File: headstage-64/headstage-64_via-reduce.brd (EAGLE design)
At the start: 19.3 x 19 mm, 172 parts, among them U1 TS4231, U11 10M08DC, U12 LT3463, U13 DAC5311, U14 TS4231, U15 INA826, U16 TLV70733, U17 TLV70712, U18 TLV70733, U19 DS90UB913A_WQFN, U2 MPU9250_QFN_NO-PAD, U22 TPS62621, U25 TPL0501_UQFN, U26 ASCO-50.000MHZ-EK-T3, U3 CAT4016_QFN, U4 OPA170, U5 TS4231, U6 TS4231, U7 RHD2064_BGA, U8 ADG1401, U9 TLV70725

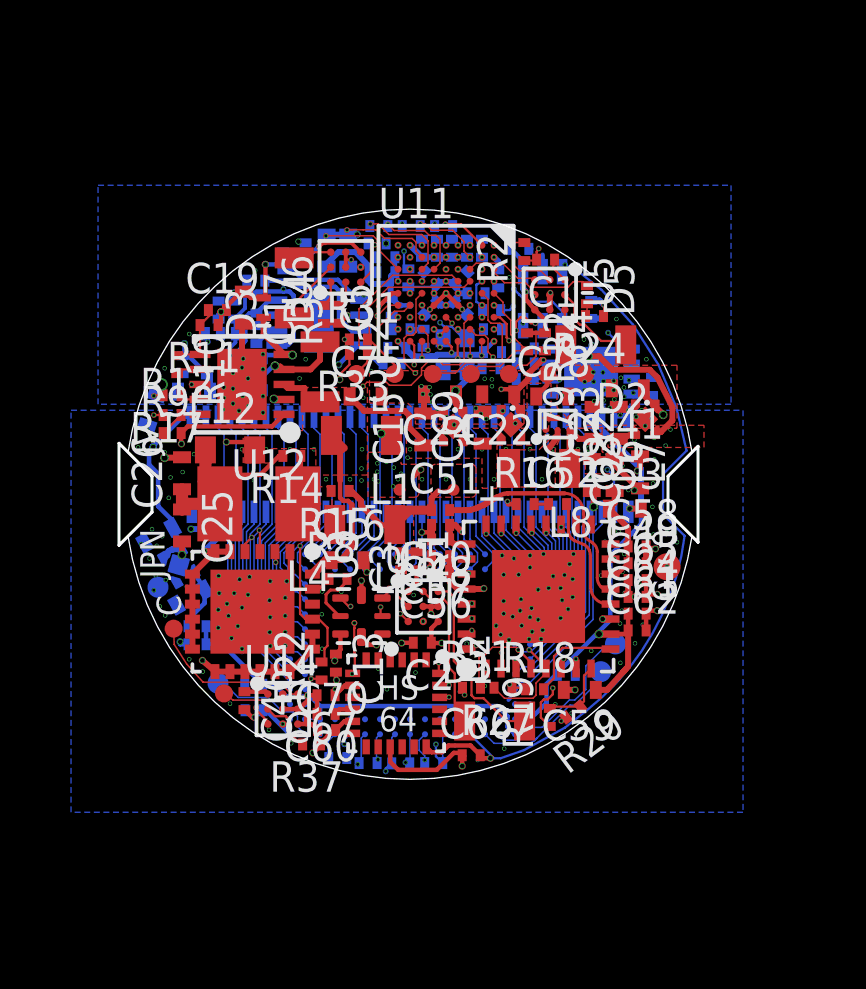
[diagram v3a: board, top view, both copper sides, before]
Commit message: Finalizing headstage-64
- Jon's final edits before fab
- Daughter board switched to IPEC4 coax connector
- RF grounding improvements: controlled impedance on daughter board and
mainboard.
- Lots of small routing improvments for DRC etc
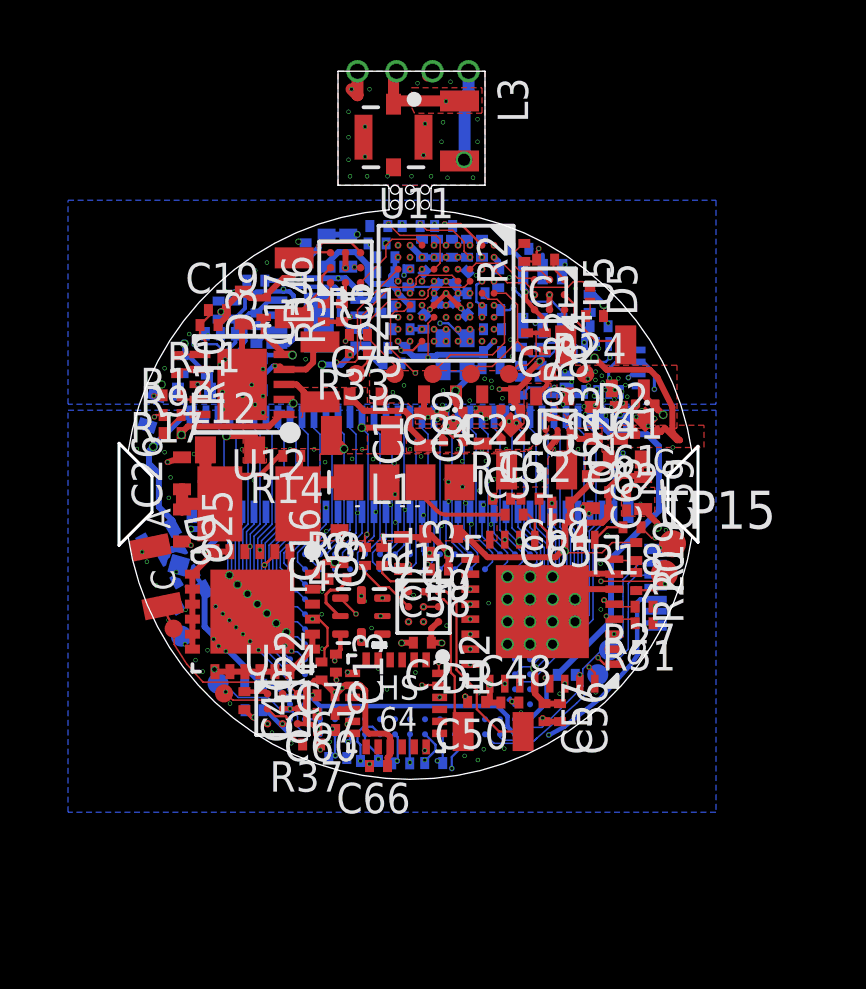
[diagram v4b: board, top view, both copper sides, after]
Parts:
- removed CENTER, SHIELD: (no value), jonnew:B0.4MM
- removed R39: 0 (DNP), jonnew:0201T
- removed R40: 0, jonnew:0201T
- added D6: VEMD1160X01, jonnew:0805T
- added J1: (no value), jonnew:X_FL_R_SMT_1(02)
- added J2: (no value), jonnew:HEADSTAGE64-DAUGHER-CARD-CASTELLATED
- added J3: (no value), jonnew:HEADSTAGE-64-DAUGHTER-CARD
- added R25: 10k, jonnew:0201T
- added TP15: (no value), jonnew:TP09R
- added U$54: PINHD-1X5_HALF_CONNETOR, jonnew:DF40-10HEAD_HALF
- R13: value 49.9 -> 590
- U8: value ADG1401 -> DG509B; device jonnew:LFCSP8-2X3 -> jonnew:MQFN16-1.8X2.6
- moved R15 13.6 mm to (1.52, 13.1), flipped to the bottom
- moved L3 13.5 mm to (1.65, 12.1), turned to 270 degrees
- moved C53 7.54 mm to (-0.23, -1.96), turned to 270 degrees
- moved C59 6.89 mm to (7.77, 0.04), turned to 270 degrees
- moved C58 6.63 mm to (0.98, -2.51), turned to 180 degrees
- moved C49 6.60 mm to (0.98, -1.95), turned to 180 degrees
- moved R18 6.30 mm to (7.40, -1.10), turned to 180 degrees
- moved C57 6.26 mm to (4.48, -7.28), turned to 270 degrees
- moved R19 6.24 mm to (7.54, -1.91), turned to 270 degrees
- moved C56 6.18 mm to (5.00, -7.28), turned to 270 degrees
- moved R51 6.14 mm to (7.80, -4.30), turned to 180 degrees
- moved L7 6.10 mm to (1.04, -1.32), turned to 180 degrees
- moved C50 6.02 mm to (2.22, -6.92)
- moved C48 5.91 mm to (3.33, -6.94), turned to 0 degrees
- moved R27 5.42 mm to (7.80, -3.75)
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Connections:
- net RHD_CLK_+ renamed RHD_CLK_P
- net RHD_CLK_- renamed RHD_CLK_N
- net RHD_CS_+ renamed RHD_CS_P
- net RHD_CS_- renamed RHD_CS_N
- net RHD_MISO_+ renamed RHD_MISO_P
- net RHD_MISO_- renamed RHD_MISO_N
- net RHD_MOSI_+ renamed RHD_MOSI_P
- net RHD_MOSI_- renamed RHD_MOSI_N
- removed net INTAN_VDD: C73.2, R39.1, R40.2, U7.M15, U7.M16, U7.N15, U7.N2
- removed net V+: C10.1, C18.1, C20.1, C7.1, R9.2, U12.1, U15.8, U4.5, U8.4
- removed net V-: C11.1, C17.1, C19.2, C21.1, C8.1, D4.A, R11.1, U15.5, U15.PAD, U4.2, U8.7, U8.PAD
- new net +15V: C10.1, C18.1, C20.1, C7.1, R9.2, U12.1, U15.8, U4.5, U8.12
- new net -15V: C11.1, C17.1, C19.2, C21.1, C8.1, D4.A, R11.1, U15.5, U15.PAD, U4.2, U8.1
- new net GND1: J1.P$2, J1.P$3, J1.P$4, J2.2, J2.4
- new net ISTIM_MONO: C9.1, R4.1, R5.2, U4.3, U7.N5
- new net ISTIM_PRE: R7.1, U15.1, U8.7
- new net N$44: R25.2, U8.16
- new net _SIGOUT: J1.P$1, J2.3, L3.1, R15.1
- net +3V3: now also R25.1; no longer R39.2
- net +3V3_AN: now also C73.2, U$54.4, U7.M15, U7.M16, U7.N15, U7.N2; no longer R40.1
- net AGND: now also U$54.M1, U$54.M2
- net AUXIN2: now also U$54.2
- net AUXIN3: now also U$54.1
- net DIN10: now also U11.C5; no longer U11.F8
- net DIN11: now also U11.C4; no longer U11.F9
- net DIN4: now also U11.G8; no longer U11.J7
- net DIN5: now also U11.G9; no longer U11.J8
- net DIN6: now also U11.F7; no longer U11.G7
- net DIN7: now also U11.E7; no longer U11.F7
- net DIN8: now also U11.E8; no longer U11.G8
- net DIN9: now also U11.C8; no longer U11.G9
- net ENV1: now also U11.B5; no longer U11.E8
- net ENV4: now also U11.B7; no longer U11.G3
- net GND: now also J3.2, J3.4, TP15.TP, U8.13, U8.14, U8.2; no longer SHIELD.TP, U8.3
- net GPIO0: now also U$54.3
- net HSYNC: now also U11.F2; no longer U11.B7
- net IMU_CS: now also U11.F9; no longer U11.A3
- net ISTIM: now also U8.10, U8.6; no longer R7.1, U15.1, U8.1
- net LED_BLANK: now also U11.C9; no longer U11.C5
- net LED_CLK: now also U11.J7; no longer U11.F2
- net LED_LATCH: now also U11.J8; no longer U11.G2
- net MIDFILT: now also J3.1; no longer L3.2, R15.2
- net N$23: now also U8.11; no longer U8.8
- net N$25: now also J2.1, L3.2, R15.2; no longer C9.1, R4.1, R5.2, U4.3
- net N$26: now also D6.2
- net N$38: now also D6.1
- net PCLK: now also U11.G2; no longer U11.C9
- net POT_CS: now also U11.G7; no longer U11.G1
- net SCL: now also U11.G3; no longer U11.C8
- net SDA: now also U11.F8; no longer U11.E7
- net SDI: now also U11.C7; no longer U11.B5
- net SIGOUT: now also J3.3; no longer CENTER.TP, L3.1, R15.1
- net STIM_NULL: now also U11.A3, U8.15; no longer U11.C4, U8.6
- net VDAC: no longer U7.N5
- net VSYNC: now also U11.G1; no longer U11.C7
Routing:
- net +15V: track 0.00 -> 35.2 mm, vias 0 -> 4
- net V+: track 34.1 -> 0.00 mm, vias 4 -> 0
- net ISTIM_MONO: track 0.00 -> 29.4 mm, vias 0 -> 3
- net GPIO0: track 18.8 -> 44.0 mm, vias 3 -> 4
- net VDAC: track 38.2 -> 15.4 mm
- net V-: track 22.3 -> 0.00 mm, vias 4 -> 0
- net +3V3_AN: track 2.15 -> 23.2 mm, vias 0 -> 2
- net -15V: track 0.00 -> 20.7 mm, vias 0 -> 4
- net ENV1: track 13.8 -> 34.4 mm
- net DIN9: track 11.7 -> 31.6 mm
- net ISTIM_PRE: track 0.00 -> 19.4 mm, vias 0 -> 2
- net DIN8: track 11.1 -> 30.4 mm
- net DIN7: track 10.4 -> 28.2 mm
- net ISTIM: track 25.5 -> 8.72 mm, vias 3 -> 2
- net DATA1: track 14.3 -> 30.8 mm, vias 3 -> 2
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- added copper zone on layer 7, net $N324
- added copper zone on layer 1, net +15V
- added copper zone on layer 16, net +15V
- added copper zone on layer 3, net +15V
- added copper zone on layer 7, net +1V2
- added copper zone on layer 7, net +2V5
- added copper zone on layer 7, net +3V3
- added copper zone on layer 16, net +3V3_AN
- added copper zone on layer 7, net +3V3_AN
- added copper zone on layer 1, net -15V
- added copper zone on layer 16, net -15V
- added copper zone on layer 3, net -15V
- added copper zone on layer 7, net AGND
- added copper zone on layer 5, net DAC_CS
- added copper zone on layer 5, net DATA4
- added copper zone on layer 5, net DIN0
- added copper zone on layer 5, net DIN1
- added copper zone on layer 5, net DIN10
- added copper zone on layer 5, net DIN11
- added copper zone on layer 5, net DIN2
- added copper zone on layer 5, net DIN3
- added copper zone on layer 5, net DIN4
- added copper zone on layer 5, net DIN5
- added copper zone on layer 5, net DIN6
- added copper zone on layer 5, net DIN7
- added copper zone on layer 5, net DIN8
- added copper zone on layer 5, net DIN9
- added copper zone on layer 3, net ENV1
- added copper zone on layer 5, net ENV2
- added copper zone on layer 5, net ENV3
- added copper zone on layer 5, net ENV4
- added copper zone on layer 2, net GND
- added copper zone on layer 6, net GND
- added copper zone on layer 1, net GND1
- added copper zone on layer 16, net GND1
- added copper zone on layer 4, net GND1
- added copper zone on layer 7, net GND1
- added copper zone on layer 16, net GPIO0
- added copper zone on layer 5, net GPIO0
- added copper zone on layer 5, net HSYNC
- added copper zone on layer 5, net IMU_CS
- added copper zone on layer 5, net ISTIM
- added copper zone on layer 16, net ISTIM_MONO
- added copper zone on layer 3, net ISTIM_MONO
- added copper zone on layer 5, net ISTIM_MONO
- added copper zone on layer 16, net ISTIM_PRE
- added copper zone on layer 3, net ISTIM_PRE
- added copper zone on layer 5, net LED_BLANK
- added copper zone on layer 5, net LED_CLK
- added copper zone on layer 5, net LED_LATCH
- added copper zone on layer 16, net N$23
- added copper zone on layer 7, net N$23
- added copper zone on layer 1, net N$25
- added copper zone on layer 16, net N$25
- added copper zone on layer 1, net N$35
- added copper zone on layer 3, net N$35
- added copper zone on layer 5, net N$37
- added copper zone on layer 1, net N$38
- added copper zone on layer 5, net N$38
- added copper zone on layer 1, net N$43
- added copper zone on layer 4, net N$43
- added copper zone on layer 5, net N$45
- added copper zone on layer 2, net N$47
- added copper zone on layer 3, net N$47
- added copper zone on layer 4, net N$47
- added copper zone on layer 5, net PCLK
- added copper zone on layer 5, net POT_CS
- added copper zone on layer 3, net RHD_CLK_N
- added copper zone on layer 5, net RHD_CLK_N
- added copper zone on layer 3, net RHD_CLK_P
- added copper zone on layer 5, net RHD_CLK_P
- added copper zone on layer 3, net RHD_CS_N
- added copper zone on layer 3, net RHD_CS_P
- added copper zone on layer 3, net RHD_MISO_N
- added copper zone on layer 3, net RHD_MISO_P
- added copper zone on layer 3, net RHD_MOSI_N
- added copper zone on layer 3, net RHD_MOSI_P
- added copper zone on layer 5, net SCL
- added copper zone on layer 3, net SDA
- added copper zone on layer 5, net SDI
- added copper zone on layer 5, net STIM_NULL
- added copper zone on layer 5, net VCOAX
- added copper zone on layer 7, net VDAC
- added copper zone on layer 5, net VSYNC
- added copper zone on layer 1, net _SIGOUT
- added copper zone on layer 16, net _SIGOUT
- removed copper zone on layer 5, net $N324
- removed copper zone on layer 5, net +1V2
- removed copper zone on layer 5, net +3V3
- removed copper zone on layer 5, net AGND
- removed copper zone on layer 2, net DAC_CS
- removed copper zone on layer 1, net DATA1
- removed copper zone on layer 2, net DATA1
- removed copper zone on layer 1, net DATA3
- removed copper zone on layer 2, net DATA3
- removed copper zone on layer 2, net DATA4
- removed copper zone on layer 1, net DIN0
- removed copper zone on layer 2, net DIN0
- removed copper zone on layer 1, net DIN1
- removed copper zone on layer 2, net DIN1
- removed copper zone on layer 2, net DIN10
- removed copper zone on layer 2, net DIN11
- removed copper zone on layer 2, net DIN2
- removed copper zone on layer 1, net DIN3
- removed copper zone on layer 2, net DIN3
- removed copper zone on layer 1, net DIN4
- removed copper zone on layer 2, net DIN4
- removed copper zone on layer 1, net DIN5
- removed copper zone on layer 2, net DIN5
- removed copper zone on layer 2, net DIN6
- removed copper zone on layer 1, net DIN7
- removed copper zone on layer 2, net DIN7
- removed copper zone on layer 2, net DIN8
- removed copper zone on layer 1, net DIN9
- removed copper zone on layer 2, net DIN9
- removed copper zone on layer 2, net ENV1
- removed copper zone on layer 1, net ENV2
- removed copper zone on layer 2, net ENV2
- removed copper zone on layer 2, net ENV3
- removed copper zone on layer 1, net ENV4
- removed copper zone on layer 2, net ENV4
- removed copper zone on layer 3, net ENV4
- removed copper zone on layer 2, net GPIO0
- removed copper zone on layer 3, net GPIO0
- removed copper zone on layer 2, net HSYNC
- removed copper zone on layer 1, net IMU_CS
- removed copper zone on layer 3, net IMU_CS
- removed copper zone on layer 3, net ISTIM
- removed copper zone on layer 3, net LED_BLANK
- removed copper zone on layer 3, net LED_CLK
- removed copper zone on layer 3, net LED_LATCH
- removed copper zone on layer 1, net MIDFILT
- removed copper zone on layer 2, net MOSI
- removed copper zone on layer 1, net N$34
- removed copper zone on layer 3, net N$34
- removed copper zone on layer 2, net N$37
- removed copper zone on layer 3, net N$43
- removed copper zone on layer 2, net N$45
- removed copper zone on layer 2, net PCLK
- removed copper zone on layer 1, net POT_CS
- removed copper zone on layer 2, net POT_CS
- removed copper zone on layer 3, net POT_CS
- removed copper zone on layer 1, net RHD_CLK_N
- removed copper zone on layer 2, net RHD_CLK_N
- removed copper zone on layer 2, net RHD_CLK_P
- removed copper zone on layer 1, net RHD_CS_N
- removed copper zone on layer 2, net RHD_CS_N
- removed copper zone on layer 1, net RHD_CS_P
- removed copper zone on layer 2, net RHD_CS_P
- removed copper zone on layer 1, net RHD_MISO_N
- removed copper zone on layer 2, net RHD_MISO_N
- removed copper zone on layer 1, net RHD_MISO_P
- removed copper zone on layer 2, net RHD_MISO_P
- removed copper zone on layer 1, net RHD_MOSI_N
- removed copper zone on layer 2, net RHD_MOSI_N
- removed copper zone on layer 1, net RHD_MOSI_P
- removed copper zone on layer 2, net RHD_MOSI_P
- removed copper zone on layer 2, net SCL
- removed copper zone on layer 2, net SCLK
- removed copper zone on layer 2, net SDA
- removed copper zone on layer 2, net SDI
- removed copper zone on layer 1, net SIGOUT
- removed copper zone on layer 2, net STIM_NULL
- removed copper zone on layer 1, net V+
- removed copper zone on layer 16, net V+
- removed copper zone on layer 3, net V+
- removed copper zone on layer 1, net V-
- removed copper zone on layer 16, net V-
- removed copper zone on layer 3, net V-
- removed copper zone on layer 5, net VDAC
- removed copper zone on layer 2, net VSYNC
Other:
- board size 19.3 x 19 mm -> 19.3 x 23.6 mm
- board text added: "3"
- board text added: "A"
- board text added: "HS 64 JPN&JV"
- board text removed: "+"
- board text removed: "-"
- board text removed: "IN3"
- board text removed: "JPN"
- board text removed: "JV"

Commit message: headstage-64 ready for fabrication
- Ready for speedy
- Tiny improvements due to DRC and drill rack check
- Fabrication files updated
- Missing gerber files added
- Gerbv project updated
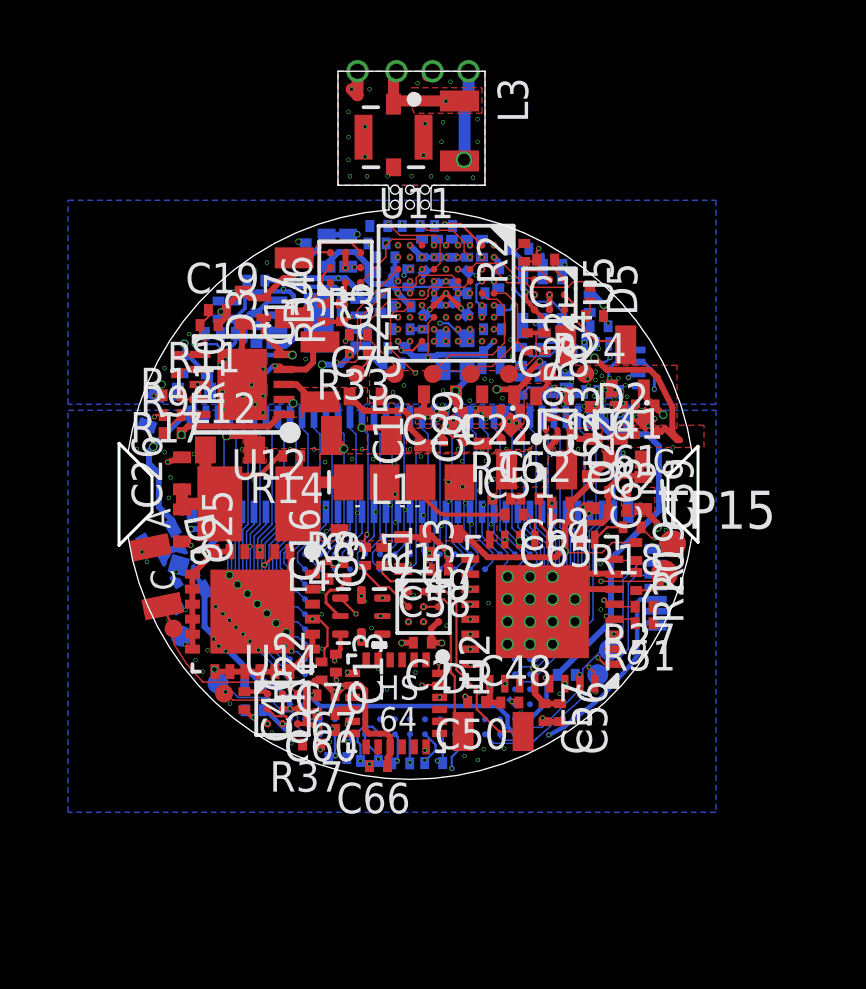
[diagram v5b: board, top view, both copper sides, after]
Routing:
- net GND: vias 201 -> 200
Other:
- board text added: "HS-64 Rev 1.2"
- board text removed: "HS-64 Rev 1.1"

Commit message: Moved parts around on headstage-64 to increase spaces between pads
- Tried to jiggle parts around to prevent very closely spaced pads on
difference signals. Hopefully this will reduce possibily of shorts
during reflow.
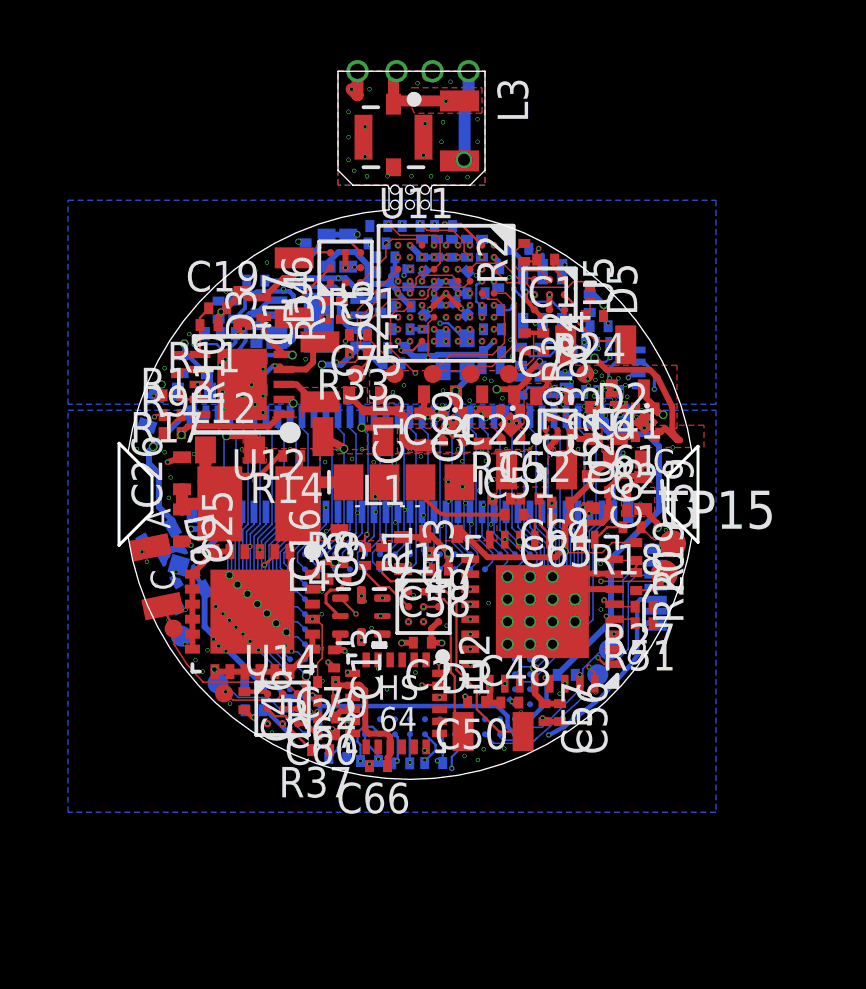
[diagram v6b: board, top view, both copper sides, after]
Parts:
- moved R22 0.41 mm to (-2.78, -6.26), turned to 180 degrees
- moved R37 0.36 mm to (-2.98, -8.53)
- moved L1 0.28 mm to (-1.90, 1.92)
- moved C67 0.18 mm to (-2.78, -6.88)
- moved C13 0.15 mm to (-2.53, -5.49)
- moved C70 0.14 mm to (-2.78, -8.00)
- moved C60 0.12 mm to (-2.78, -7.44)
- moved U17 0.10 mm to (7.84, 2.40)
- moved C5 0.10 mm to (-2.83, 6.14)
- moved R3 0.08 mm to (-2.27, 6.13)
- moved R32 0.07 mm to (3.83, 5.08)
- moved C19 0.06 mm to (-6.41, 6.20)
- moved C17 0.05 mm to (-5.59, 6.21)
- moved C4 0.05 mm to (4.44, 5.08)
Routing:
- net GND: track 29.4 -> 27.8 mm, vias 200 -> 204
- net +3V3: track 37.7 -> 38.4 mm
- net LED_BLANK: track 16.4 -> 17.2 mm
- net N$17: track 1.49 -> 0.82 mm
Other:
- outline, holes or cut-outs redrawn

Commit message: Many fixes on headstage-64 before fabriation
- A bit of scary commit because I found significant errors in the board
- There were redunant MOSI lines and a missing MISO line for the IMU.
These were fixed. The extra line allowed GPIO1 from serializer to be
routed to FPGA.
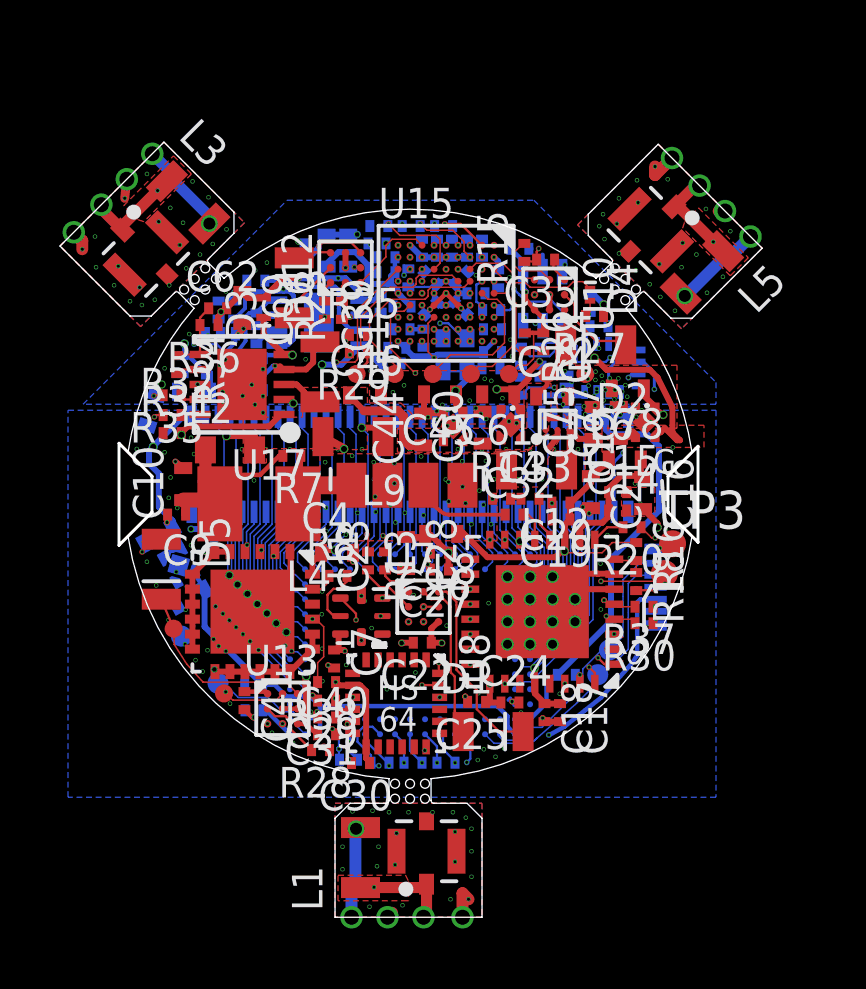
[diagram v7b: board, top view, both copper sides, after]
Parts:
- removed C79: 4.7uF, jonnew:0402T
- removed L13: BLM15PX601SN1D, jonnew:0402T
- removed R50: 100, jonnew:0201T
- removed R51: 4.7k, jonnew:0201T
- removed U22: TPS62621, jonnew:XBGA6_1.2X0.8
- removed U25: TPL0501_UQFN, jonnew:UQFN
- added C55: 4.7nF, jonnew:0201T
- added J4, J7: (no value), jonnew:HEADSTAGE64-DAUGHER-CARD-CASTELLATED
- added J5: (no value), jonnew:HEADSTAGE-64-DAUGHTER-CARD
- added J6: (no value), jonnew:X_FL_R_SMT_1(02)
- added L10: BLM15PX601SN1D, jonnew:0402T
- added L11, L9: MLZ2012M100WT000, jonnew:0805T
- added R39, R40, R41, R42: 10k, jonnew:0201T
- added U10: TS4231, jonnew:WLCSP3X3
- added U21: TLV70712, jonnew:X2SON
- C1: value 1uF -> 470pF
- C10, C21: value 0.1uF -> 4.7uF; device jonnew:0201T -> jonnew:0402T
- C14, C76: value 1uF -> 10nF; device jonnew:0402T -> jonnew:0201T
- C15: value 1uF -> 0.1uF; device jonnew:0402T -> jonnew:0201T
- C16, C75: value 1uF -> 4.7uF
- C17: value 0.22uF -> 0.1uF; device jonnew:0402T -> jonnew:0201T
- C18: value 0.22uF -> 10nF; device jonnew:0402T -> jonnew:0201T
- C19: value 10pF -> 10nF
- C22, C24: value 10uF -> 0.1uF; device jonnew:0402T -> jonnew:0201T
- C23: device jonnew:0402T -> jonnew:0201T
- C25: value 4.7uF -> 10nF; device jonnew:0402T -> jonnew:0201T
- C26: value 0.1uF -> 10nF; device jonnew:0402T -> jonnew:0201T
- C27, C38: value 10nF -> 0.1uF
- C28: value 47nF -> 22uF; device jonnew:0201T -> jonnew:0402T
- C29, C31, C32, C37: value 4.7nF -> 0.1uF
- C3, C5: value 1uF -> 0.1uF
- C33: value 22nF -> 47nF
- C34: value 47nF -> 0.1uF
- C35: value 2.2nF -> 1uF
- C36, C56, C64: value 0.1uF -> 10nF
- C39: value 22nF -> 1uF
- C4, C60: value 0.1uF -> 1uF; device jonnew:0201T -> jonnew:0402T
- C40: value 0.47uF -> 0.1uF
- C41: value 22uF -> 1uF; device jonnew:0402T -> jonnew:0201T
- C42, C77: value 10uF -> 1uF
- C43: value 10nF -> 10uF; device jonnew:0201T -> jonnew:0402T
- C44: value 22nF -> 1uF; device jonnew:0201T -> jonnew:0402T
- C45: value 0.47uF -> 10uF; device jonnew:0201T -> jonnew:0402T
- C46, C68: device jonnew:0201T -> jonnew:0402T
- C47: value 10nF -> 0.22uF; device jonnew:0201T -> jonnew:0402T
- C48: value 0.1uF -> 2.2nF
- C49: value 10nF -> 4.7nF
- C51: value 0.1uF -> 22nF
- C53: value 22uF -> 0.1uF; device jonnew:0402T -> jonnew:0201T
- C54: value 10nF -> 1uF
- C57, C65: value 10nF -> 22nF
- C58, C67, C73: value 0.1uF -> 0.47uF
- C59: value 4.7uF -> 10uF
- C6: value 0.1uF -> 1uF
- C61: value 0.1uF -> 10uF; device jonnew:0201T -> jonnew:0402T
- C62: value 10nF -> 10pF
- C63: value 4.7uF -> 4.7nF; device jonnew:0402T -> jonnew:0201T
- C66: value 10nF -> 47nF
- C69: value 1uF -> 0.22uF
- C70: value 0.1uF -> 4.7nF
- C71: value 22nF -> 10nF
- C72: value 0.47uF -> 22nF
- C74: value 1uF -> 2.2uF; device jonnew:0201T -> jonnew:0402T
- C78: value 2.2uF -> 22uF
- C9: value 470pF -> 0.1uF
- D1, D2, D3: device jonnew:0805T -> jonnew:0805PT
- D4: value VSKY05401006 -> XZVGR155W; device jonnew:CLP1006-2L -> jonnew:LED-0201T
- D5: value XZVGR155W -> VEMD1160X01; device jonnew:LED-0201T -> jonnew:0805PT
- D6: value VEMD1160X01 -> VSKY05401006; device jonnew:0805T -> jonnew:CLP1006-2L
- J3: device jonnew:HEADSTAGE-64-DAUGHTER-CARD -> jonnew:X_FL_R_SMT_1(02)
- L1: value MLZ2012M100WT000 -> CIG21L4R7MNE
- L12: value BLM18KG601SN1D -> LQM21PN1R0NGRD; device jonnew:0603T -> jonnew:0805T
- L2: value MLZ2012M100WT000 -> BLM18KG601SN1D; device jonnew:0805T -> jonnew:0603T
- L5: value BLM15PX601SN1D -> CIG21L4R7MNE; device jonnew:0402T -> jonnew:0805T
- L8: value LQM21PN1R0NGRD -> BLM15PX601SN1D; device jonnew:0805T -> jonnew:0402T
- R1, R2: value 15k -> 10k
- R10: value 83.3k -> 590
- R11: value 1M -> 10k
- R12: value 90.9k -> 10k
- R13: value 590 -> 15k
- R14: value 1k -> 49.9
- R15: value 1k -> 15k
- R16: value 49.9 -> 10k
- R17: value 10k -> 0
- R18: value 10k -> 100k
- R19, R22: value 10k -> 100
- R20: value 100k -> 10k
- R21: value 0 -> 100
- R23: value 10k -> 15k
- R24: value 2k -> 10k
- R26: value 100 -> 10k
- R27: value 4.7k -> 2k
- R28: value 100 -> 15k
- R29: value 100 -> 1k
- R3: value 15k -> 1k
- R30: value 10k -> 4.7k
- R31, R36: value 10k -> 1M
- R32: value 10k -> 90.9k
- R33: value 1k -> 100
- R34: value 10k -> 83.3k
- R37: value 15k -> 4.7k
- R4: value 10k -> 220
- R5: value 10k -> 5.49k
- R6: value 5.49k -> 1k
- R7: value 220 -> 1k
- R9: value 1M -> 1k
- TP1: device jonnew:TP06R -> jonnew:TP07R
- TP10, TP13, TP8: value VCC -> (none); device jonnew:TP07R -> jonnew:TP06R
- TP14: value VCC -> gnd; device jonnew:TP07R -> jonnew:TP06R
- TP15: value (none) -> VCC; device jonnew:TP09R -> jonnew:TP06R
- TP2: value gnd -> VCC; device jonnew:TP06R -> jonnew:TP07R
- TP3, TP4: device jonnew:TP06R -> jonnew:TP09R
- TP5, TP6: value (none) -> VCC; device jonnew:TP06R -> jonnew:TP07R
- TP7: device jonnew:TP09R -> jonnew:TP06R
- U1: value TS4231 -> CAT4016_QFN; device jonnew:WLCSP3X3 -> jonnew:QFN24-4X4
- U11: value 10M08DC -> DS90UB913A_WQFN; device jonnew:VBGA81-4X4 -> jonnew:WQFN32-5X5
- U12: value LT3463 -> TS4231; device jonnew:DFN103X3 -> jonnew:WLCSP3X3
- U13: value DAC5311 -> TS4231; device jonnew:SC70 -> jonnew:WLCSP3X3
- U14: value TS4231 -> TLV70733; device jonnew:WLCSP3X3 -> jonnew:X2SON
- U15: value INA826 -> 10M08DC; device jonnew:PWSON-N8-3X3 -> jonnew:VBGA81-4X4
- U17: value TLV70712 -> LT3463; device jonnew:X2SON -> jonnew:DFN103X3
- U18: value TLV70733 -> TLV70725
- U19: value DS90UB913A_WQFN -> TPS62621; device jonnew:WQFN32-5X5 -> jonnew:XBGA6_1.2X0.8
- U2: value MPU9250_QFN_NO-PAD -> OPA170; device jonnew:QFN24-3X3_NO-PAD -> jonnew:PDSO-N5
- U3: value CAT4016_QFN -> INA826; device jonnew:QFN24-4X4 -> jonnew:PWSON-N8-3X3
- U4: value OPA170 -> DAC5311; device jonnew:PDSO-N5 -> jonnew:SC70
- U5: value TS4231 -> TPL0501_UQFN; device jonnew:WLCSP3X3 -> jonnew:UQFN
- U6: value TS4231 -> DG509B; device jonnew:WLCSP3X3 -> jonnew:MQFN16-1.8X2.6
- U7: value RHD2064_BGA -> TS4231; device jonnew:BGA104_0.5MM -> jonnew:WLCSP3X3
- U8: value DG509B -> MPU9250_QFN_NO-PAD; device jonnew:MQFN16-1.8X2.6 -> jonnew:QFN24-3X3_NO-PAD
- U9: value TLV70725 -> RHD2064_BGA; device jonnew:X2SON -> jonnew:BGA104_0.5MM
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- renumbered U$1 to J8, U$54 to J9, U26 to U20
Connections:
- removed net +15V: C10.1, C18.1, C20.1, C7.1, R9.2, U12.1, U15.8, U4.5, U8.12
- removed net -15V: C11.1, C17.1, C19.2, C21.1, C8.1, D4.A, R11.1, U15.5, U15.PAD, U4.2, U8.1
- removed net LED_CLK: U11.J7, U3.3
- removed net SDI: U11.C7, U2.24, U25.P$2
- new net +15V0: C12.1, C2.1, C3.1, C47.1, R31.2, U17.1, U2.5, U3.8, U6.12
- new net -15V0: C11.1, C13.1, C62.2, C69.1, C8.1, D6.A, R36.1, U2.2, U3.5, U3.PAD, U6.1
- new net GND2: J1.P$2, J1.P$3, J1.P$4, J2.2, J2.4
- new net GND3: J6.P$2, J6.P$3, J6.P$4, J7.2, J7.4
- new net GPIO1: U11.16, U15.H6
- new net MISO: U15.E3, U8.9
- new net N$48: J2.1, L1.2, R3.2
- new net N$50: J7.1, L5.2, R9.2
- new net _SIGOUT1: J1.P$1, J2.3, L1.1, R3.1
- new net _SIGOUT2: J6.P$1, J7.3, L5.1, R9.1
- net $N324: now also C55.1, C56.1, C57.1, C58.1, C59.1, L10.2, U15.A8; no longer C37.1, C38.1, C39.1, C40.1, C42.1, L5.2, U11.A8
- net +1V2: now also C48.1, C49.1, C50.1, C51.1, C52.1, C53.1, C54.1, C78.1, L10.1, U15.B2, U15.B9, U15.H2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; no longer C27.1, C29.1, C33.1, C34.1, C35.1, C36.1, C41.1, C68.1, L5.1, U11.B2, U11.B9, U11.H2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
- net +1V8: now also C17.1, C18.1, C19.1, C20.1, C21.1, C75.1, L12.1, R16.1, U11.11, U11.28, U19.C1; no longer C56.1, C57.1, C63.1, C64.1, C65.1, C79.1, L7.1, R19.1, U19.11, U19.28, U22.C1
- net +2V5: now also C61.1, C70.1, C73.1, C77.1, U15.B1, U15.B8, U15.J1, U15.J9, U18.1, U21.3, U21.4; no longer C22.1, C23.1, C32.1, C47.1, U11.B1, U11.B8, U11.J1, U11.J9, U17.3, U17.4, U9.1
- net +3V3: now also C22.1, C25.1, C29.1, C30.1, C34.1, C38.1, C40.1, C5.1, C63.1, C64.1, C65.1, C7.1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; no longer C12.1, C13.1, C2.1, C28.1, C31.1, C4.1, C43.1, C44.1, C48.1, C50.1, C54.1, C70.1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
- net +3V3_AN: now also C37.2, C43.1, U14.1, U9.M15, U9.M16, U9.N15, U9.N2; no longer C73.2, C77.1, U16.1, U7.M15, U7.M16, U7.N15, U7.N2
- net AGND: now also C36.2, C37.1, C42.2, C43.2, L7.2, R17.1, TP1.TP, U14.2, U14.PAD, U9.M17, U9.M2, U9.N1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; no longer C30.2, C73.1, C76.2, C77.2, L13.2, R21.1, TP14.TP, U16.2, U16.PAD, U7.M17, U7.M2, U7.N1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
- net AUXIN2: now also TP6.TP, U9.N4; no longer TP10.TP, U7.N4
- net AUXIN3: now also TP5.TP, U9.N3; no longer TP8.TP, U7.N3
- net CONFIG_SEL: now also R42.1, U15.C6; no longer R34.1, U11.C6
- net CONF_DONE: now also R41.2, U15.A2; no longer R36.2, U11.A2
- net DAC_CS: now also U15.C2, U4.1; no longer U11.C2, U13.1
- net DATA1: now also U15.C7, U7.C1; no longer U1.C1, U11.A4
- net DATA2: now also U10.C1, U15.C3; no longer U11.C3, U5.C1
- net DATA3: now also U12.C1, U15.A7; no longer U11.A7, U6.C1
- net DATA4: now also U13.C1, U15.B6; no longer U11.B6, U14.C1
- net DIN0: now also U11.19, U15.J6; no longer U11.H6, U19.19
- net DIN1: now also U11.20, U15.G6; no longer U11.J6, U19.20
- net DIN10: now also U11.31, U15.C5; no longer U11.C5, U19.31
- net DIN11: now also U11.32, U15.C4; no longer U11.C4, U19.32
- net DIN2: now also U11.21, U15.H7; no longer U11.G6, U19.21
- net DIN3: now also U11.22, U15.J7; no longer U11.H7, U19.22
- net DIN4: now also U11.23, U15.G8; no longer U11.G8, U19.23
- net DIN5: now also U11.24, U15.G9; no longer U11.G9, U19.24
- net DIN6: now also U11.26, U15.F7; no longer U11.F7, U19.26
- net DIN7: now also U11.27, U15.E7; no longer U11.E7, U19.27
- net DIN8: now also U11.29, U15.E8; no longer U11.E8, U19.29
- net DIN9: now also U11.30, U15.C8; no longer U11.C8, U19.30
- net E0: now also U9.K2; no longer U7.K2
- net E1: now also U9.J1; no longer U7.J1
- net E10: now also U9.E2; no longer U7.E2
- net E11: now also U9.D1; no longer U7.D1
- net E12: now also U9.D2; no longer U7.D2
- net E13: now also U9.C1; no longer U7.C1
- net E14: now also U9.C2; no longer U7.C2
- net E15: now also U9.B1; no longer U7.B1
- net E16: now also U9.A1; no longer U7.A1
- net E17: now also U9.B2; no longer U7.B2
- net E18: now also U9.A2; no longer U7.A2
- net E19: now also U9.B3; no longer U7.B3
- net E2: now also U9.J2; no longer U7.J2
- net E20: now also U9.A3; no longer U7.A3
- net E21: now also U9.B4; no longer U7.B4
- net E22: now also U9.A4; no longer U7.A4
- net E23: now also U9.B5; no longer U7.B5
- net E24: now also U9.A5; no longer U7.A5
- net E25: now also U9.B6; no longer U7.B6
- net E26: now also U9.A6; no longer U7.A6
- net E27: now also U9.B7; no longer U7.B7
- net E28: now also U9.A7; no longer U7.A7
- net E29: now also U9.B8; no longer U7.B8
- net E3: now also U9.H1; no longer U7.H1
- net E30: now also U9.A8; no longer U7.A8
- net E31: now also U9.B9; no longer U7.B9
- net E32: now also U9.A9; no longer U7.A9
- net E33: now also U9.A10; no longer U7.A10
- net E34: now also U9.B10; no longer U7.B10
- net E35: now also U9.A11; no longer U7.A11
- net E36: now also U9.B11; no longer U7.B11
- net E37: now also U9.A12; no longer U7.A12
- net E38: now also U9.B12; no longer U7.B12
- net E39: now also U9.A13; no longer U7.A13
- net E4: now also U9.H2; no longer U7.H2
- net E40: now also U9.B13; no longer U7.B13
- net E41: now also U9.A14; no longer U7.A14
- net E42: now also U9.B14; no longer U7.B14
- net E43: now also U9.A15; no longer U7.A15
- net E44: now also U9.B15; no longer U7.B15
- net E45: now also U9.A16; no longer U7.A16
- net E46: now also U9.B16; no longer U7.B16
- net E47: now also U9.A17; no longer U7.A17
- net E48: now also U9.B17; no longer U7.B17
- net E49: now also U9.C16; no longer U7.C16
- net E5: now also U9.G1; no longer U7.G1
- net E50: now also U9.C17; no longer U7.C17
- net E51: now also U9.D16; no longer U7.D16
- net E52: now also U9.D17; no longer U7.D17
- net E53: now also U9.E16; no longer U7.E16
- net E54: now also U9.E17; no longer U7.E17
- net E55: now also U9.F16; no longer U7.F16
- net E56: now also U9.F17; no longer U7.F17
- net E57: now also U9.G16; no longer U7.G16
- net E58: now also U9.G17; no longer U7.G17
- net E59: now also U9.H16; no longer U7.H16
- net E6: now also U9.G2; no longer U7.G2
- net E60: now also U9.H17; no longer U7.H17
- net E61: now also U9.J16; no longer U7.J16
- net E62: now also U9.J17; no longer U7.J17
- net E63: now also U9.K16; no longer U7.K16
- net E7: now also U9.F1; no longer U7.F1
- net E8: now also U9.F2; no longer U7.F2
- net E9: now also U9.E1; no longer U7.E1
- net ENV1: now also U15.B5, U7.C2; no longer U1.C2, U11.B5
- net ENV2: now also U10.C2, U15.F1; no longer U11.F1, U5.C2
- net ENV3: now also U12.C2, U15.D9; no longer U11.D9, U6.C2
- net ENV4: now also U13.C2, U15.B7; no longer U11.B7, U14.C2
- net ESTIM_POW_EN: now also R35.1, U15.A6, U17.8, U17.9; no longer R17.1, U11.A6, U12.8, U12.9
- net GND: now also C14.2, C19.2, C30.2, C51.2, C52.2, C55.2, C73.2, C76.2, C77.2, C9.2, J5.2, J5.4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; no longer C1.2, C32.2, C33.2, C36.2, C37.2, C42.2, C43.2, C62.2, C68.2, C79.2, J3.2, J3.4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
- net GND1: now also J3.P$2, J3.P$3, J3.P$4, J4.2, J4.4; no longer J1.P$2, J1.P$3, J1.P$4, J2.2, J2.4
- net GPIO0: now also TP4.TP, U11.15, U15.A5; no longer TP7.TP, U11.A5, U19.15
- net HSYNC: now also U11.1, U15.F2; no longer U11.F2, U19.1
- net IMU_CS: now also U15.F9, U8.22; no longer U11.F9, U2.22
- net ISTIM: now also U6.10, U6.6; no longer U8.10, U8.6
- net ISTIM_MONO: now also C1.1, R1.2, R2.1, U2.3, U9.N5; no longer C9.1, R4.1, R5.2, U4.3, U7.N5
- net ISTIM_PRE: now also R4.1, U3.1, U6.7; no longer R7.1, U15.1, U8.7
- net JTAGEN: now also R24.2, U15.D2; no longer R30.2, U11.D2
- net LED-1: now also U1.10, U1.11, U1.12, U1.5, U1.6, U1.7, U1.8, U1.9; no longer U3.10, U3.11, U3.12, U3.5, U3.6, U3.7, U3.8, U3.9
- net LED-2: now also U1.13, U1.14, U1.15, U1.16, U1.17, U1.18, U1.19, U1.20; no longer U3.13, U3.14, U3.15, U3.16, U3.17, U3.18, U3.19, U3.20
- net LED_BLANK: now also R38.2, U1.21, U15.C9; no longer R22.2, U11.C9, U3.21
- net LED_LATCH: now also U1.4, U15.J8; no longer U11.J8, U3.4
- net MIDFILT: now also J5.1, R7.1; no longer J3.1, R14.1
- net MOSI: now also U1.2, U15.A4, U4.3, U5.P$2, U8.24; no longer U11.E3, U13.3, U2.9, U3.2
- net N$1: now also U5.P$6; no longer U25.P$6
- net N$10: now also D2.A, U10.A2; no longer D2.1, U5.A2
- net N$11: now also R15.2, U10.B1; no longer R2.2, U5.B1
- net N$12: now also C35.1, U10.A1; no longer C1.1, U5.A1
- net N$13: now also C10.1, C9.1, L2.1, R7.2; no longer C25.1, C26.1, L12.1, R14.2
- net N$14: now also U1.23; no longer U3.23
- net N$15: now also D3.C, U12.A3; no longer D3.2, U6.A3
- net N$16: now also D3.A, U12.A2; no longer D3.1, U6.A2
- net N$17: now also R23.2, U12.B1; no longer R3.2, U6.B1
- net N$18: now also C39.1, U12.A1; no longer C5.1, U6.A1
- net N$19: now also C68.2, D6.C, U17.5; no longer C14.2, D4.C, U12.5
- net N$2: now also C68.1, L11.1, U17.4; no longer C14.1, L2.1, U12.4
- net N$20: now also R5.2, U3.2; no longer R6.2, U15.2
- net N$21: now also R5.1, U3.3; no longer R6.1, U15.3
- net N$22: now also C1.2, R4.2, U2.4, U3.4; no longer C9.2, R7.2, U15.4, U4.4
- net N$23: now also R10.2, U6.11; no longer R13.2, U8.11
- net N$24: now also R31.1, R32.2, U17.10; no longer R12.2, R9.1, U12.10
- net N$25: now also J4.1, R6.2; no longer J2.1, R15.2
- net N$26: now also D5.C, TP7.TP, U13.A3; no longer D6.2, TP9.TP, U14.A3
- net N$27: now also R34.2, U17.7; no longer R10.2, U12.7
- net N$28: now also C32.2, U11.13; no longer C51.2, U19.13
- net N$29: now also D4.2, R27.2; no longer D5.2, R24.2
- net N$3: now also C62.1, R34.1, R36.2, U17.6; no longer C19.1, R10.1, R11.2, U12.6
- net N$30: now also R20.2, U11.9; no longer R18.2, U19.9
- net N$31: now also C33.2, U11.12; no longer C52.2, U19.12
- net N$32: now also C33.1, R14.2; no longer C52.1, R16.2
- net N$33: now also R16.2, R18.1, U11.8; no longer R19.2, R20.1, U19.8
- net N$34: now also C14.1, C15.1, C16.1, U11.10; no longer C59.1, C61.1, C62.1, U19.10
- net N$35: now also C26.1, C27.1, C28.1, L8.2, U11.14; no longer C49.1, C53.1, C58.1, L7.2, U19.14
- net N$36: now also C36.1, U9.N17; no longer C30.1, U7.N17
- net N$37: now also U15.D8; no longer U11.D8
- net N$38: now also D5.A, TP8.TP, U13.A2; no longer D6.1, TP11.TP, U14.A2
- net N$39: now also TP2.TP, U9.N16; no longer TP13.TP, U7.N16
- net N$4: now also D1.C, U7.A3; no longer D1.2, U1.A3
- net N$40: now also C31.1, U8.10; no longer C60.1, U2.10
- net N$41: now also R28.2, U13.B1; no longer R37.2, U14.B1
- net N$42: now also C41.1, U13.A1; no longer C46.1, U14.A1
- net N$44: now also R11.2, U6.16; no longer R25.2, U8.16
- net N$45: now also R39.2, U15.D6; no longer R38.2, U11.D6
- net N$46: now also L12.2, U19.B1; no longer L8.2, U22.B1
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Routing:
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- added copper zone on layer 1, net +15V0
- added copper zone on layer 16, net +15V0
- added copper zone on layer 3, net +15V0
- added copper zone on layer 1, net -15V0
- added copper zone on layer 16, net -15V0
- added copper zone on layer 3, net -15V0
- added copper zone on layer 1, net DIN1
- added copper zone on layer 1, net GND2
- added copper zone on layer 16, net GND2
- added copper zone on layer 4, net GND2
- added copper zone on layer 7, net GND2
- added copper zone on layer 1, net GND3
- added copper zone on layer 16, net GND3
- added copper zone on layer 4, net GND3
- added copper zone on layer 7, net GND3
- added copper zone on layer 5, net GPIO1
- added copper zone on layer 3, net MISO
- added copper zone on layer 5, net MISO
- added copper zone on layer 5, net MOSI
- added copper zone on layer 1, net N$48
- added copper zone on layer 16, net N$48
- added copper zone on layer 1, net N$49
- added copper zone on layer 4, net N$49
- added copper zone on layer 1, net N$50
- added copper zone on layer 16, net N$50
- added copper zone on layer 1, net N$51
- added copper zone on layer 4, net N$51
- added copper zone on layer 1, net _SIGOUT1
- added copper zone on layer 16, net _SIGOUT1
- added copper zone on layer 1, net _SIGOUT2
- added copper zone on layer 16, net _SIGOUT2
- removed copper zone on layer 1, net +15V
- removed copper zone on layer 16, net +15V
- removed copper zone on layer 3, net +15V
- removed copper zone on layer 1, net -15V
- removed copper zone on layer 16, net -15V
- removed copper zone on layer 3, net -15V
- removed copper zone on layer 1, net DIN2
- removed copper zone on layer 1, net LED_CLK
- removed copper zone on layer 5, net LED_CLK
- removed copper zone on layer 1, net N$25
- removed copper zone on layer 1, net SDI
- removed copper zone on layer 3, net SDI
- removed copper zone on layer 5, net SDI
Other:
- board size 19.3 x 23.6 mm -> 23.4 x 25.8 mm
- board text removed: "A"
- board text removed: "C"
